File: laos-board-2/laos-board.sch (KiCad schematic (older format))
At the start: 93 parts, among them IC1 KB847, IC2 KB847, J1 USB-A, J10 CONN_4, J11 MBED NXP, J12 JP, J13 JP_3, J14 CONN_4, J15 JP, J16 JP_3, J17 POLOLU1201, J18 CONN_5, J19 JP, J2 CONN_4, J20 JP_3, J21 JP, J22 JP_3, J23 POLOLU1201, J24 CONN_5, J25 JP, J26 JP_3, J27 CONN_4, J28 JP3, J29 CONN_4, J3 JP, J30 JP, J31 JP_3, J32 POLOLU1201, J33 CONN_5, J34 CONN_4, J35 JP, J36 JP_3, J37 CONN_4, J38 CONN_2, J39 CONN_4, J4 MAGJACK, J5 CONN_2, J6 JP, J7 JP_3, J8 POLOLU1201, J9 CONN_5, Q1 TIP115, Q2 TIP115, U1 65HVD251, U2 SDCARD, U3 7805

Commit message: schematic updates to work toward rev.2
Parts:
- added J?: JP, symbol JP
- C7: value 33nF -> 22nF
- R2, R23, R24, R26, R27, R3: value 470R -> 1K
- R28, R29, R31, R32: value 2k -> 330R
- R7, R8: value 2k -> 2K2
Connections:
- net labels removed: +5VD
- wire segments 398 -> 405
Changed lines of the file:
@@
-EESchema Schematic File Version 2  date Fri 15 Jul 2011 10:05:13 AM CEST
+EESchema Schematic File Version 2  date Tue 20 Sep 2011 03:18:05 PM CEST
 LIBS:laos_kicad_lib
 LIBS:laos-board-cache
@@
 Sheet 1 1
 Title "LAOS"
-Date "15 jul 2011"
+Date "20 sep 2011"
 Rev "1"
 Comp "http://www.laoslaser.org"
@@
 Comment4 ""
 $EndDescr
+Wire Wire Line
+	11440 1435 11440 1560
+Connection ~ 5400 770
+Wire Wire Line
+	5400 770  5200 770
+Wire Wire Line
+	5200 770  5200 1300
+Wire Wire Line
+	3000 3200 3000 3300
+Wire Wire Line
+	3000 3300 1650 3300
+Connection ~ 8870 6900
+Wire Wire Line
+	8865 6905 8870 6900
+Connection ~ 8980 6800
+Wire Wire Line
+	8980 6800 8980 7330
+Wire Wire Line
+	8980 7330 10260 7330
+Connection ~ 9030 8725
+Wire Wire Line
+	9030 8725 9025 9245
+Wire Wire Line
+	9025 9245 10250 9245
+Connection ~ 9180 8025
+Wire Wire Line
+	9180 8025 9180 9050
+Wire Wire Line
+	9180 9050 10260 9050
+Connection ~ 9045 3400
+Wire Wire Line
+	9045 3400 9050 3395
+Wire Wire Line
+	9050 3395 9050 3920
+Wire Wire Line
+	9050 3920 10250 3925
+Connection ~ 9030 5150
+Wire Wire Line
+	9030 5150 9030 5675
+Wire Wire Line
+	9030 5675 10250 5675
+Connection ~ 9155 4450
+Wire Wire Line
+	9155 4450 9155 5475
+Wire Wire Line
+	9155 5475 10250 5475
+Connection ~ 1850 5500
+Wire Wire Line
+	1800 5500 1850 5500
 Connection ~ 11050 8325
 Wire Wire Line
@@
 Wire Wire Line
 	10950 3200 10950 3925
-Connection ~ 8900 3500
-Wire Wire Line
-	8900 3500 8900 3825
-Wire Wire Line
-	9100 2900 9100 4025
-Connection ~ 8900 5150
-Wire Wire Line
-	8900 5150 8900 5475
-Wire Wire Line
-	8900 5475 10250 5475
-Wire Wire Line
-	9100 4550 9100 5675
-Connection ~ 8900 6900
-Wire Wire Line
-	8900 6900 8900 7225
-Wire Wire Line
-	8900 7225 10250 7225
 Wire Wire Line
 	9300 6900 7100 6900
-Connection ~ 8900 8725
-Wire Wire Line
-	8900 8725 8900 9050
-Wire Wire Line
-	8900 9050 10250 9050
-Wire Wire Line
-	9100 8125 9100 9250
 Wire Wire Line
 	2050 8700 1600 8700
@@
 	4200 5800 4100 5800
 Wire Wire Line
-	6600 4450 9300 4450
-Wire Wire Line
 	9300 5150 7400 5150
 Wire Wire Line
@@
 	8100 3250 8250 3250
 Wire Wire Line
-	10250 3925 9000 3925
-Wire Wire Line
 	8650 3000 9300 3000
 Wire Wire Line
@@
 	8650 2900 9300 2900
 Wire Wire Line
-	8900 3825 10250 3825
-Wire Wire Line
-	9100 4025 10250 4025
-Wire Wire Line
 	8550 3250 8750 3250
 Wire Wire Line
@@
 	8750 4900 8550 4900
 Wire Wire Line
-	9100 5675 10250 5675
-Connection ~ 9100 4550
-Wire Wire Line
 	8650 4550 9300 4550
 Wire Wire Line
@@
 	8650 4650 9300 4650
 Wire Wire Line
-	10250 5575 9000 5575
-Wire Wire Line
 	8250 4900 8100 4900
 Wire Wire Line
@@
 Wire Wire Line
 	8100 6650 8250 6650
-Wire Wire Line
-	10250 7325 9000 7325
 Wire Wire Line
 	8650 6400 9300 6400
@@
 Wire Wire Line
 	8650 6300 9300 6300
-Connection ~ 9100 6300
-Wire Wire Line
-	10250 7425 9100 7425
 Wire Wire Line
 	8550 6650 8750 6650
@@
 	8750 8475 8550 8475
 Wire Wire Line
-	9100 9250 10250 9250
-Connection ~ 9100 8125
-Wire Wire Line
-	8650 8125 9300 8125
-Wire Wire Line
 	9300 8325 8650 8325
 Wire Wire Line
@@
 	4200 5100 1800 5100
 Wire Wire Line
-	1650 3400 3000 3400
-Wire Wire Line
-	1650 3300 2900 3300
-Wire Wire Line
 	2550 3100 4200 3100
 Wire Wire Line
@@
 	4200 2000 1800 2000
 Connection ~ 3000 3200
-Wire Wire Line
-	3000 3400 3000 3200
 Connection ~ 8875 10075
 Wire Wire Line
@@
 Wire Wire Line
 	9275 10375 9375 10375
-Wire Wire Line
-	1850 5450 1850 5400
 Wire Wire Line
 	1700 7550 1600 7550
@@
 Wire Wire Line
 	5400 800  5400 750
-Wire Wire Line
-	5200 750  5200 1300
 Wire Wire Line
 	1475 825  1475 1025
@@
 Connection ~ 3300 10350
 Connection ~ 2300 10750
-Wire Wire Line
-	1850 5400 1800 5400
 Wire Wire Line
 	2050 4900 1800 4900
@@
 Connection ~ 8875 10375
 Wire Wire Line
-	2900 3300 2900 3100
-Connection ~ 2900 3100
-Wire Wire Line
 	2250 3100 2150 3100
 Wire Wire Line
@@
 Wire Wire Line
 	8650 8225 9300 8225
-Wire Wire Line
-	10250 9150 9000 9150
 Wire Wire Line
 	8250 8475 8100 8475
@@
 	1800 8800 1600 8800
 Connection ~ 2925 4400
-Connection ~ 9100 2900
-Wire Wire Line
-	9000 9150 9000 8625
-Connection ~ 9000 8625
-Wire Wire Line
-	9100 7425 9100 6300
-Wire Wire Line
-	9000 7325 9000 6800
-Connection ~ 9000 6800
-Wire Wire Line
-	9000 5575 9000 5050
-Connection ~ 9000 5050
 Wire Wire Line
 	9300 3400 6600 3400
-Wire Wire Line
-	9000 3925 9000 3400
-Connection ~ 9000 3400
 Wire Wire Line
 	11050 4025 11050 3100
@@
 	10950 9150 10950 8425
 Connection ~ 10950 8425
+Wire Wire Line
+	1800 5400 1850 5400
+Wire Wire Line
+	1850 5400 1850 5600
+Wire Wire Line
+	9300 4450 7300 4450
+Connection ~ 7300 4450
+Wire Wire Line
+	10245 5570 9090 5570
+Wire Wire Line
+	9090 5570 9095 5050
+Connection ~ 9095 5050
+Wire Wire Line
+	10250 3820 9150 3820
+Wire Wire Line
+	9150 3820 9150 2800
+Connection ~ 9150 2800
+Wire Wire Line
+	10250 4025 8975 4030
+Wire Wire Line
+	8975 4030 8975 3500
+Connection ~ 8975 3500
+Wire Wire Line
+	8655 8125 9295 8120
+Wire Wire Line
+	9295 8120 9300 8120
+Wire Wire Line
+	10255 9150 9095 9150
+Wire Wire Line
+	9095 9150 9095 8625
+Connection ~ 9095 8625
+Wire Wire Line
+	10245 7225 9120 7225
+Wire Wire Line
+	9120 7225 9125 6200
+Connection ~ 9125 6200
+Wire Wire Line
+	10245 7420 8870 7420
+Wire Wire Line
+	8870 7420 8870 6895
+Wire Wire Line
+	1650 3400 2925 3400
+Wire Wire Line
+	2925 3400 2925 3100
+Connection ~ 2925 3100
+Wire Wire Line
+	11440 1960 11440 2050
+Connection ~ 11440 2050
+$Comp
+L +5V #PWR?
+U 1 1 4E78913E
+P 11440 1435
+F 0 "#PWR?" H 11440 1525 20  0001 C CNN
+F 1 "+5V" H 11440 1525 30  0000 C CNN
+	1    11440 1435
+	1    0    0    -1
+$EndComp
+$Comp
+L JP J?
+U 1 1 4E7890F5
+P 11440 1760
+F 0 "J?" H 11440 1630 60  0000 C CNN
+F 1 "JP" H 11440 1875 60  0000 C CNN
+	1    11440 1760
+	0    -1   -1   0
+$EndComp
 $Comp
 L JP_3 J36
@@
 P 2400 1650
 F 0 "R3" H 2400 1750 50  0000 C CNN
-F 1 "470R" H 2400 1650 50  0000 C CNN
+F 1 "1K" H 2400 1650 50  0000 C CNN
 	1    2400 1650
 	1    0    0    -1
@@
 P 2400 1400
 F 0 "R2" H 2400 1500 50  0000 C CNN
-F 1 "470R" H 2400 1400 50  0000 C CNN
+F 1 "1K" H 2400 1400 50  0000 C CNN
 	1    2400 1400
 	1    0    0    -1
@@
 P 9125 9775
 F 0 "R28" H 9125 9875 50  0000 C CNN
-F 1 "2k" H 9125 9775 50  0000 C CNN
+F 1 "330R" H 9125 9775 50  0000 C CNN
 	1    9125 9775
 	1    0    0    -1
@@
 P 9125 10075
 F 0 "R29" H 9125 9975 50  0000 C CNN
-F 1 "2k" H 9125 10075 50  0000 C CNN
+F 1 "330R" H 9125 10075 50  0000 C CNN
 	1    9125 10075
 	1    0    0    -1
@@
 P 9125 10375
 F 0 "R31" H 9125 10275 50  0000 C CNN
-F 1 "2k" H 9125 10375 50  0000 C CNN
+F 1 "330R" H 9125 10375 50  0000 C CNN
 	1    9125 10375
 	1    0    0    -1
@@
 P 9125 10675
 F 0 "R32" H 9125 10575 50  0000 C CNN
-F 1 "2k" H 9125 10675 50  0000 C CNN
+F 1 "330R" H 9125 10675 50  0000 C CNN
 	1    9125 10675
 	1    0    0    -1
@@
 P 2200 9000
 F 0 "R27" H 2200 9100 50  0000 C CNN
-F 1 "470R" H 2200 9000 50  0000 C CNN
+F 1 "1K" H 2200 9000 50  0000 C CNN
 	1    2200 9000
 	1    0    0    -1
@@
 P 2200 8700
 F 0 "R26" H 2200 8800 50  0000 C CNN
-F 1 "470R" H 2200 8700 50  0000 C CNN
+F 1 "1K" H 2200 8700 50  0000 C CNN
 	1    2200 8700
 	1    0    0    -1
@@
 P 2200 8400
 F 0 "R24" H 2200 8500 50  0000 C CNN
-F 1 "470R" H 2200 8400 50  0000 C CNN
+F 1 "1K" H 2200 8400 50  0000 C CNN
 	1    2200 8400
 	1    0    0    -1
@@
 P 2200 8100
 F 0 "R23" H 2200 8200 50  0000 C CNN
-F 1 "470R" H 2200 8100 50  0000 C CNN
+F 1 "1K" H 2200 8100 50  0000 C CNN
 	1    2200 8100
 	1    0    0    -1
@@
 F 1 "GND" H 5400 6130 30  0001 C CNN
 	1    5400 6200
-	1    0    0    -1
-$EndComp
-$Comp
-L +5VD #PWR050
-U 1 1 4E0B1D79
-P 5200 750
-F 0 "#PWR050" H 5200 700 20  0001 C CNN
-F 1 "+5VD" H 5200 850 30  0000 C CNN
-	1    5200 750
 	1    0    0    -1
 $EndComp
@@
 L GND #PWR055
 U 1 1 4E0B1431
-P 1850 5450
-F 0 "#PWR055" H 1850 5450 30  0001 C CNN
-F 1 "GND" H 1850 5380 30  0001 C CNN
-	1    1850 5450
+P 1850 5600
+F 0 "#PWR055" H 1850 5600 30  0001 C CNN
+F 1 "GND" H 1850 5530 30  0001 C CNN
+	1    1850 5600
 	1    0    0    -1
 $EndComp
@@
 P 2400 3200
 F 0 "R8" H 2600 3250 50  0000 C CNN
-F 1 "2k" H 2400 3200 50  0000 C CNN
+F 1 "2K2" H 2400 3200 50  0000 C CNN
 	1    2400 3200
 	1    0    0    -1
@@
 P 2300 10550
 F 0 "C7" V 2400 10650 60  0000 C CNB
-F 1 "33nF" V 2200 10675 60  0000 C CNN
+F 1 "22nF" V 2200 10675 60  0000 C CNN
 F 2 "Pkg" H 2300 10325 30  0001 C CNN
 	1    2300 10550
@@
 P 2400 3100
 F 0 "R7" H 2600 3150 50  0000 C CNN
-F 1 "2k" H 2400 3100 50  0000 C CNN
+F 1 "2K2" H 2400 3100 50  0000 C CNN
 	1    2400 3100
 	1    0    0    -1

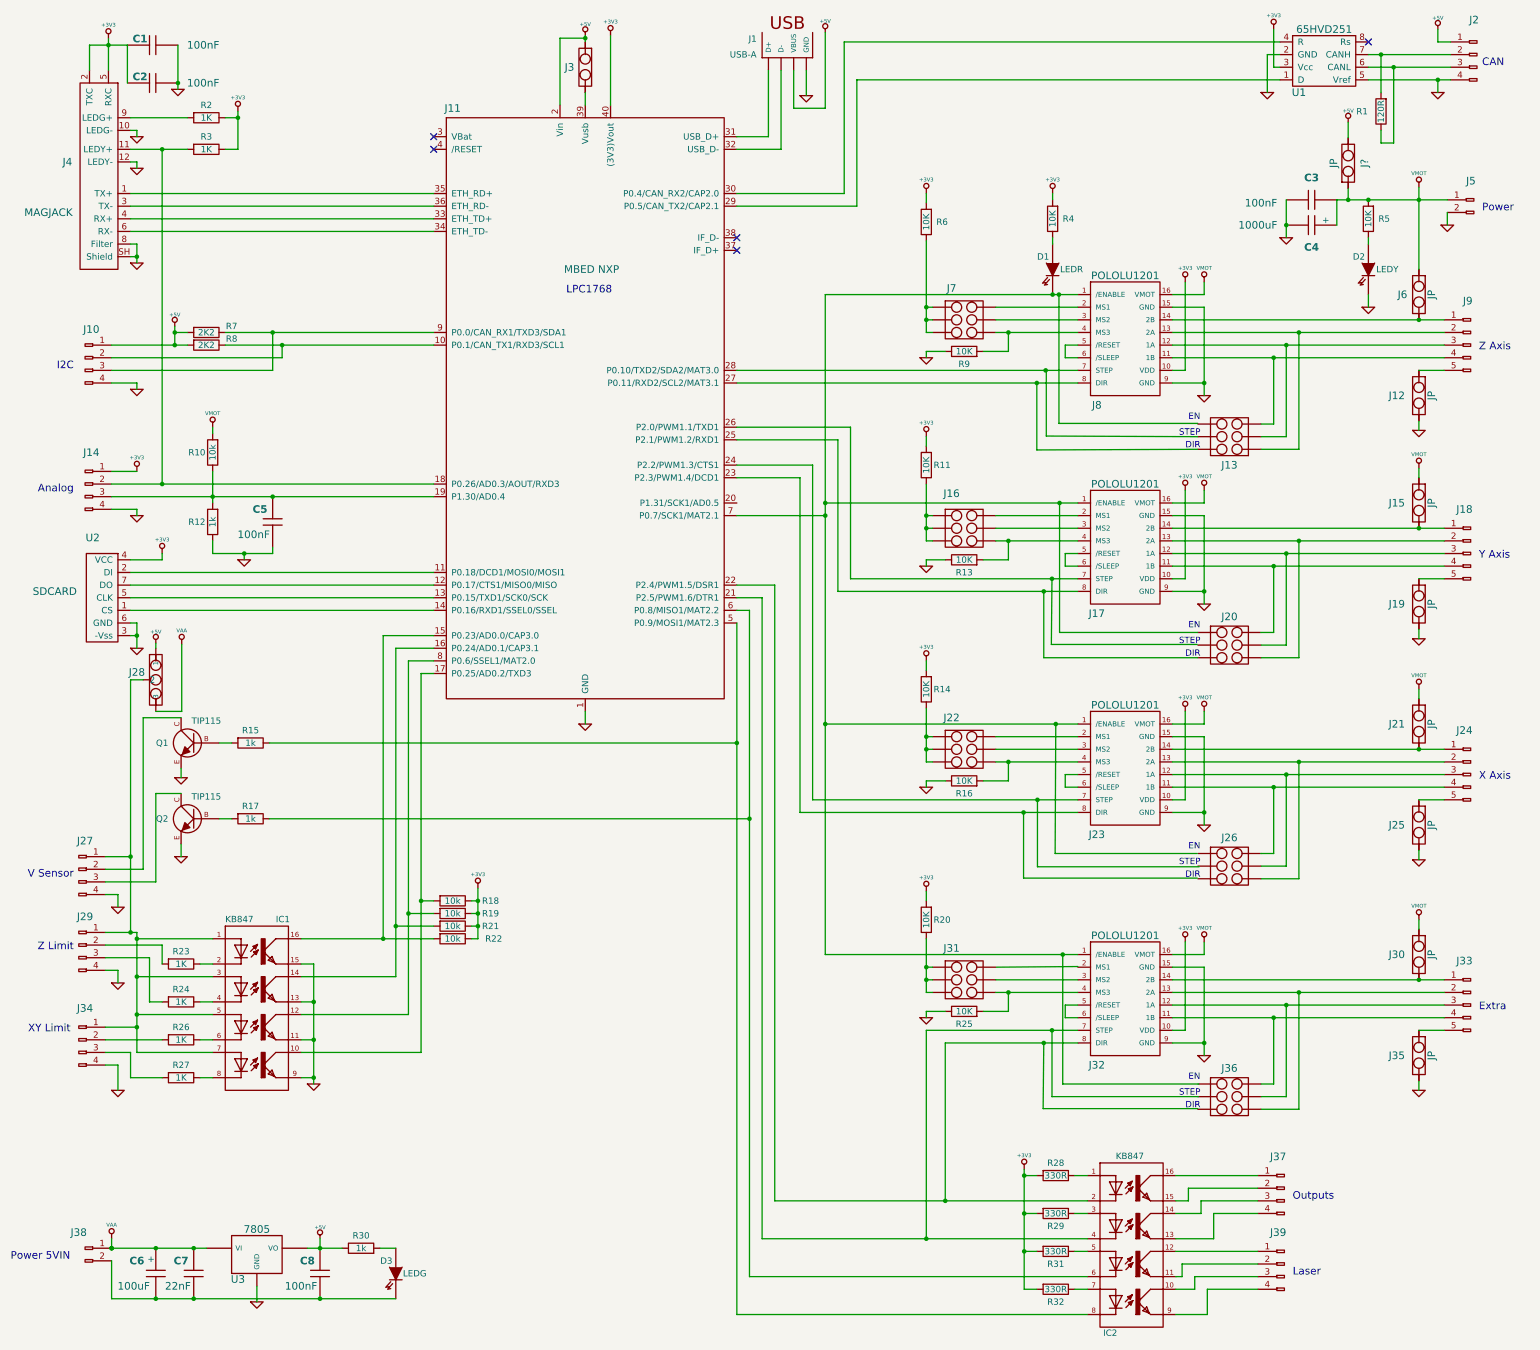
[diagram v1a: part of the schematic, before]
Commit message: nog een paar wijzigingen van het schema
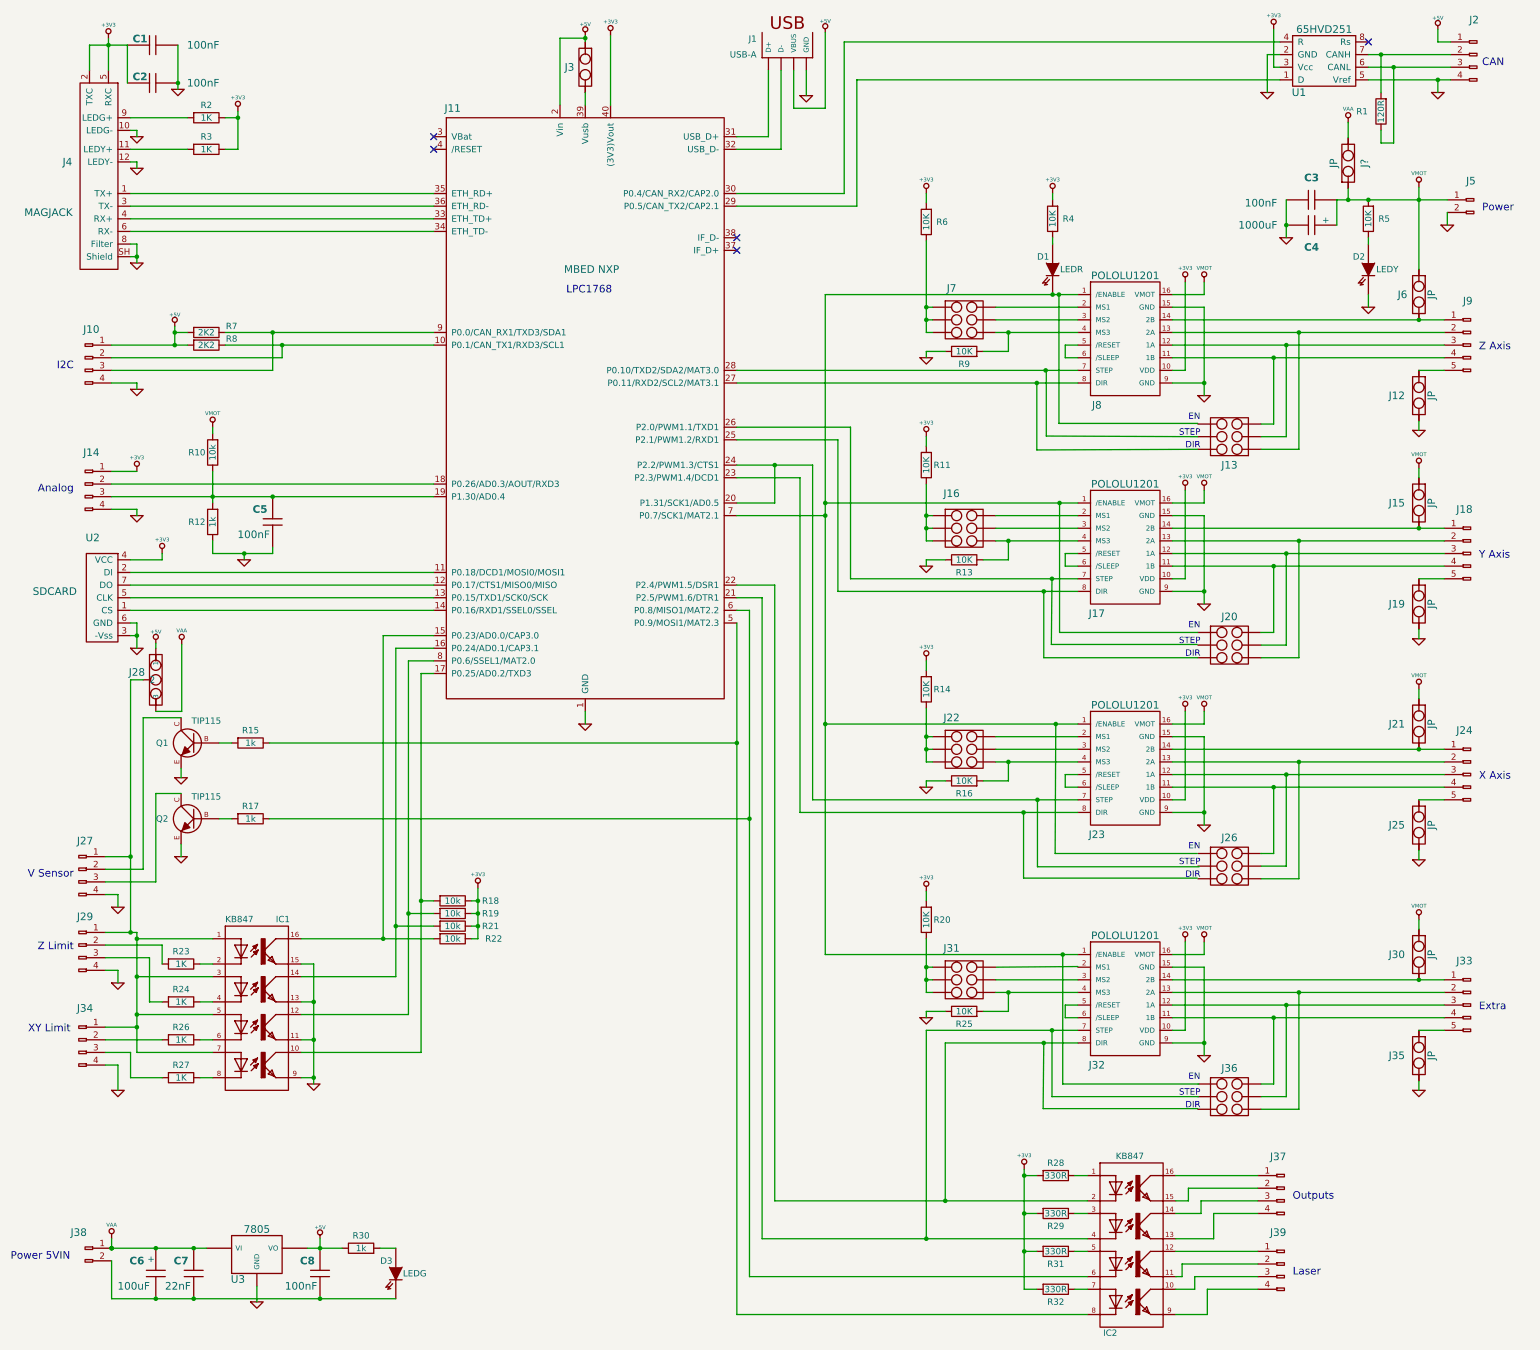
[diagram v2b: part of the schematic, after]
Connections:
- net +5V: no longer J?.2
- net at J11.18 (P0.26/AD0.3/AOUT/RXD3), J14.2 (P2): no longer J4.11 (LEDY+), R3.2
- net at J11.20 (P1.31/SCK1/AD0.5): now also J11.24 (P2.2/PWM1.3/CTS1), J23.7 (STEP)
- new net: J4.11 (LEDY+), R3.2
